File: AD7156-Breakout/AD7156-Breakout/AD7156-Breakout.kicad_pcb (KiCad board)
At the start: 2 copper layers, 13.2 x 15.7 mm, 5 parts, among them J1 Conn_01x06, J2 Cx1, J3 Cx2, U1 AD7156BCPZ-REEL7

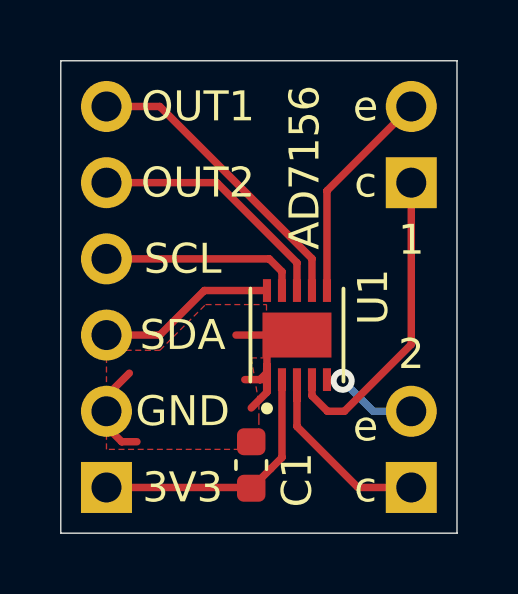
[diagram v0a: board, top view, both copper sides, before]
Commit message: Minor updates to AD7156, FDC1004Q
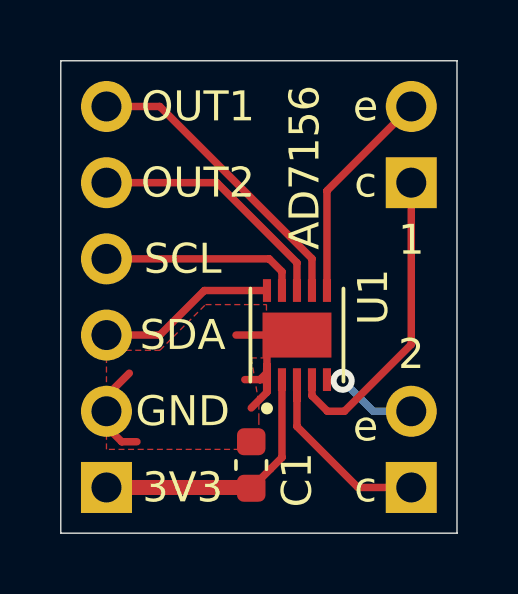
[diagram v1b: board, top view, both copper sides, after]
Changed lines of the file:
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@@
       (disableapertmacros false)
       (usegerberextensions false)
-      (usegerberattributes true)
+      (usegerberattributes false)
       (usegerberadvancedattributes true)
       (creategerberjobfile true)
@@
   (segment (start 152.12 109.22) (end 152.146 109.246) (width 0.25) (layer "F.Cu") (net 2))
   (segment (start 152.146 109.246) (end 152.146 109.22) (width 0.25) (layer "F.Cu") (net 2))
-  (segment (start 147.32 109.22) (end 152.12 109.22) (width 0.25) (layer "F.Cu") (net 2))
+  (segment (start 147.32 109.22) (end 152.12 109.22) (width 0.5) (layer "F.Cu") (net 2))
   (segment (start 153.17 105.625) (end 153.17 108.222) (width 0.25) (layer "F.Cu") (net 2))
   (segment (start 153.17 108.222) (end 152.794 108.598) (width 0.25) (layer "F.Cu") (net 2))
